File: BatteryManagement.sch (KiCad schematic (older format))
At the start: 12 parts, among them J401 Bootstrap, U401 AP9211, U402 MCP73213T-A6BI_MF

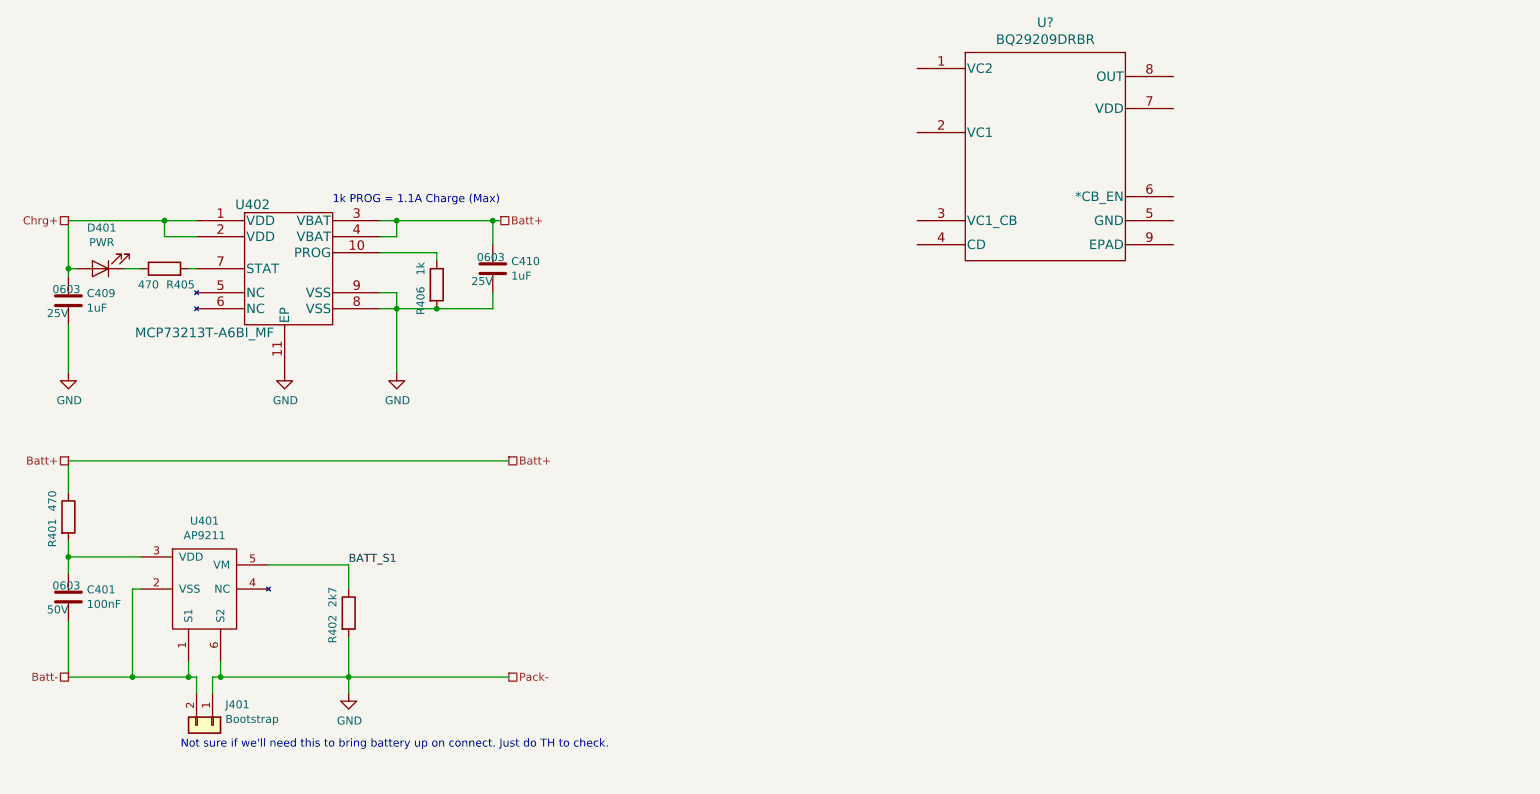
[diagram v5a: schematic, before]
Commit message: Battery circuitry nearly done. Look at charge enable.
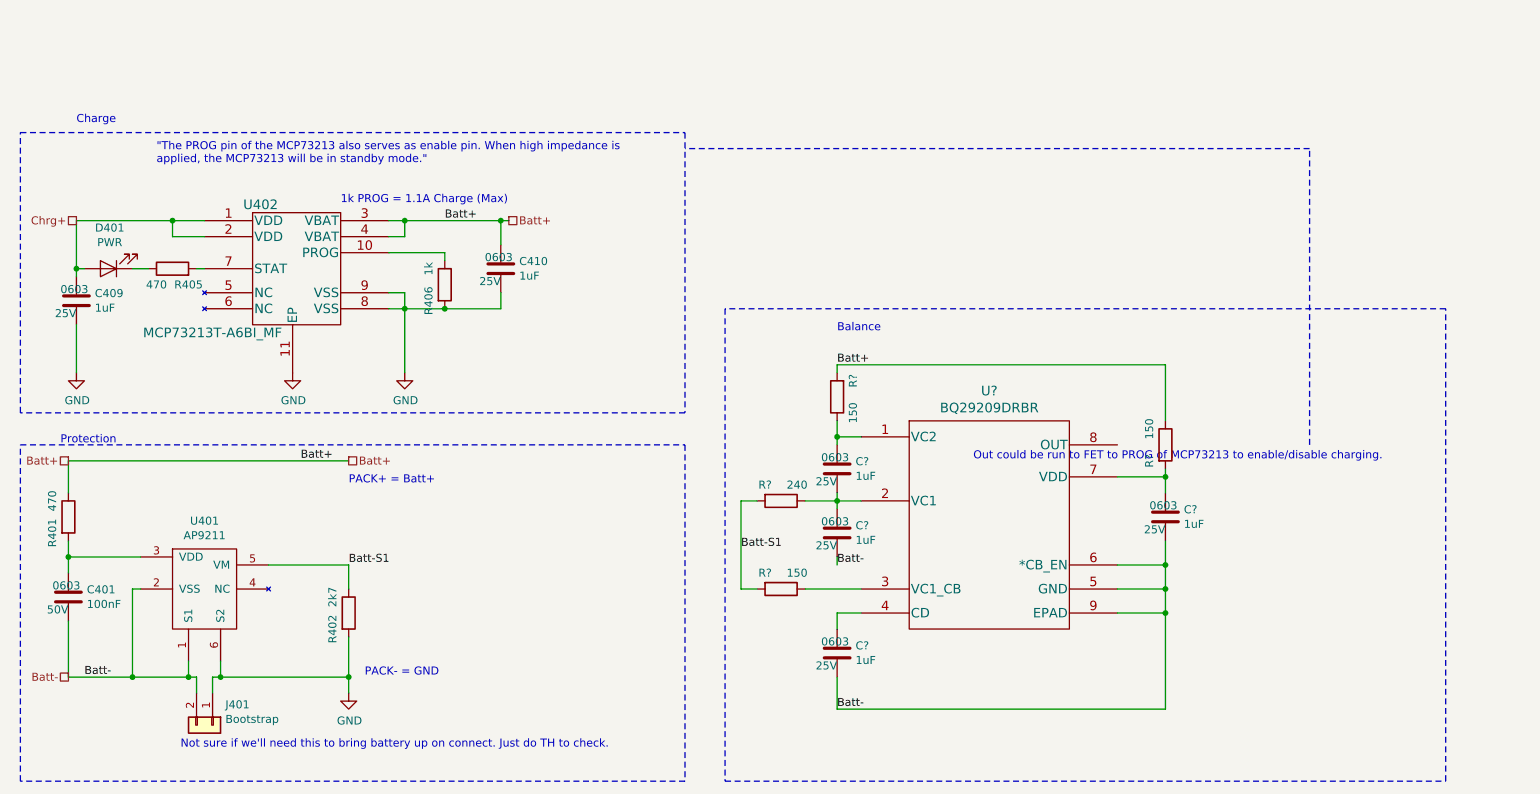
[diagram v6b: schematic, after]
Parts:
- removed U?: BQ29209DRBR, libs:BQ29209DRBR, symbol dingo-hat:BQ29209DRBR
- added C? (x4): 1uF, Capacitors_SMD:C_0603, symbol Device:C
- added R? (x3): 150, Resistors_SMD:R_0603, symbol Device:R
- added R?: 240, Resistors_SMD:R_0603, symbol Device:R
- added U?: BQ29209DRBR, DRB8_1P6X2P4, symbol dingo-hat:BQ29209DRBR
- R402, R405, R406: footprint Resistor_SMD:R_0603_1608Metric_Pad1.05x0.95mm_HandSolder -> Resistors_SMD:R_0603
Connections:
- net Batt+: now also R?.1, R?.2
- net Batt-: now also C?.2, C?.2, C?.2, U?.5 (GND), U?.6 (*CB_EN), U?.9 (EPAD)
- net BATT_S1 renamed Batt-S1
- net Batt-S1: now also R?.2, R?.2
- new net: C?.1, R?.2, U?.7 (VDD)
- new net: C?.1, C?.2, R?.1, U?.2 (VC1)
- new net: C?.1, R?.1, U?.1 (VC2)
- new net: R?.1, U?.3 (VC1_CB)
- new net: C?.1, U?.4 (CD)
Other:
- note added: ""The PROG pin of the MCP73213 also serves as enable pin. When high impedance is\napplied, the MCP73213 will be in standby mode.""
- note added: "Balance"
- note added: "Charge"
- note added: "Out could be run to FET to PROG of MCP73213 to enable/disable charging."
- note added: "PACK+ = Batt+"
- note added: "PACK- = GND"
- note added: "Protection"
- moved on the sheet: C409, C410, D401, R405, R406, U402

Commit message: Adding ADC for battery level.
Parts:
- U401: footprint (none) -> libs:6-UDFN-Exposed-Pad
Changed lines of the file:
@@
 F 0 "U401" H 2750 5525 50  0000 C CNN
 F 1 "AP9211" H 2750 5434 50  0000 C CNN
-F 2 "" H 2750 4950 50  0001 C CNN
+F 2 "libs:6-UDFN-Exposed-Pad" H 2750 4950 50  0001 C CNN
 F 3 "https://www.diodes.com/assets/Datasheets/AP9211.pdf" H 2750 4950 50  0001 C CNN
 	1    2750 5100
